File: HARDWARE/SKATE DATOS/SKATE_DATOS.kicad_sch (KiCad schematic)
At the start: 8 parts, among them J1 MPU6050, J2 BMP280, J3 ENTRADA, SW1 INTERRUPTOR, U1 ESP32-DEVKIT-V1, U2 L7805

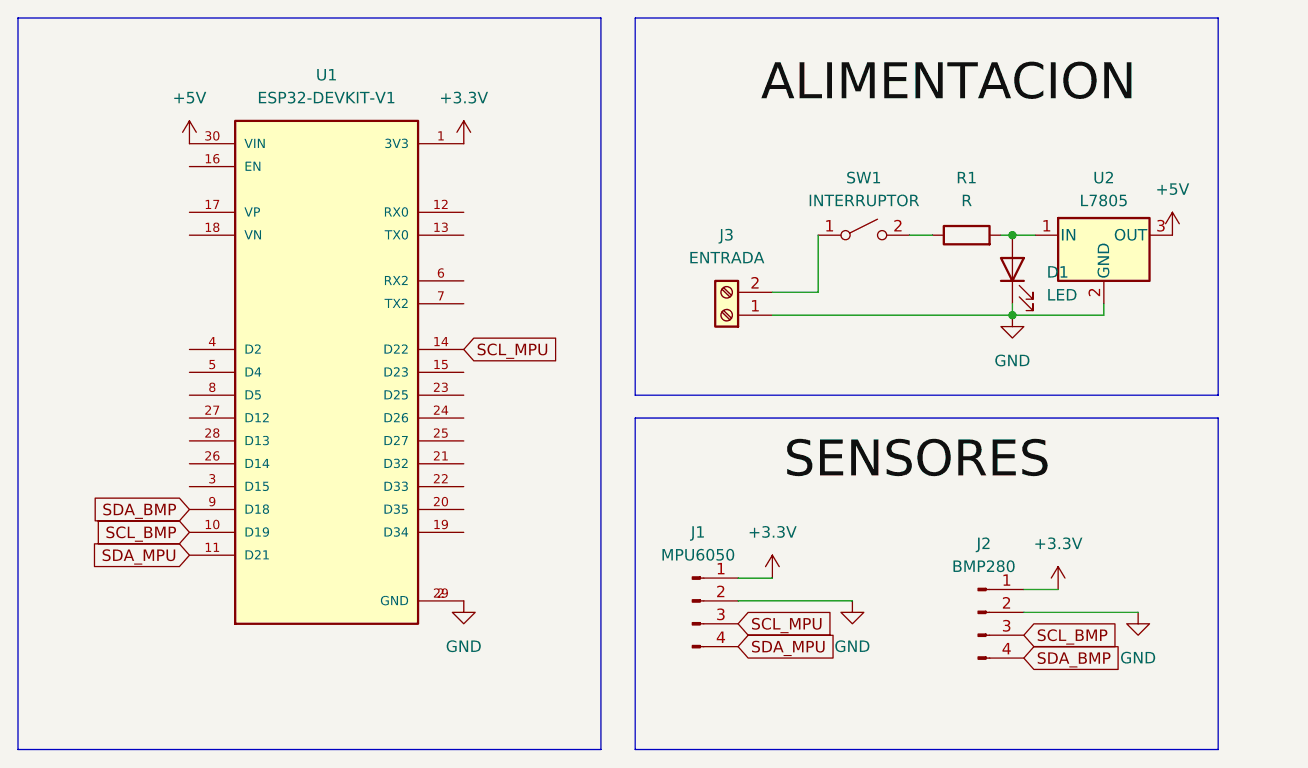
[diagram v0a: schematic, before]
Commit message: capacitores de filtro
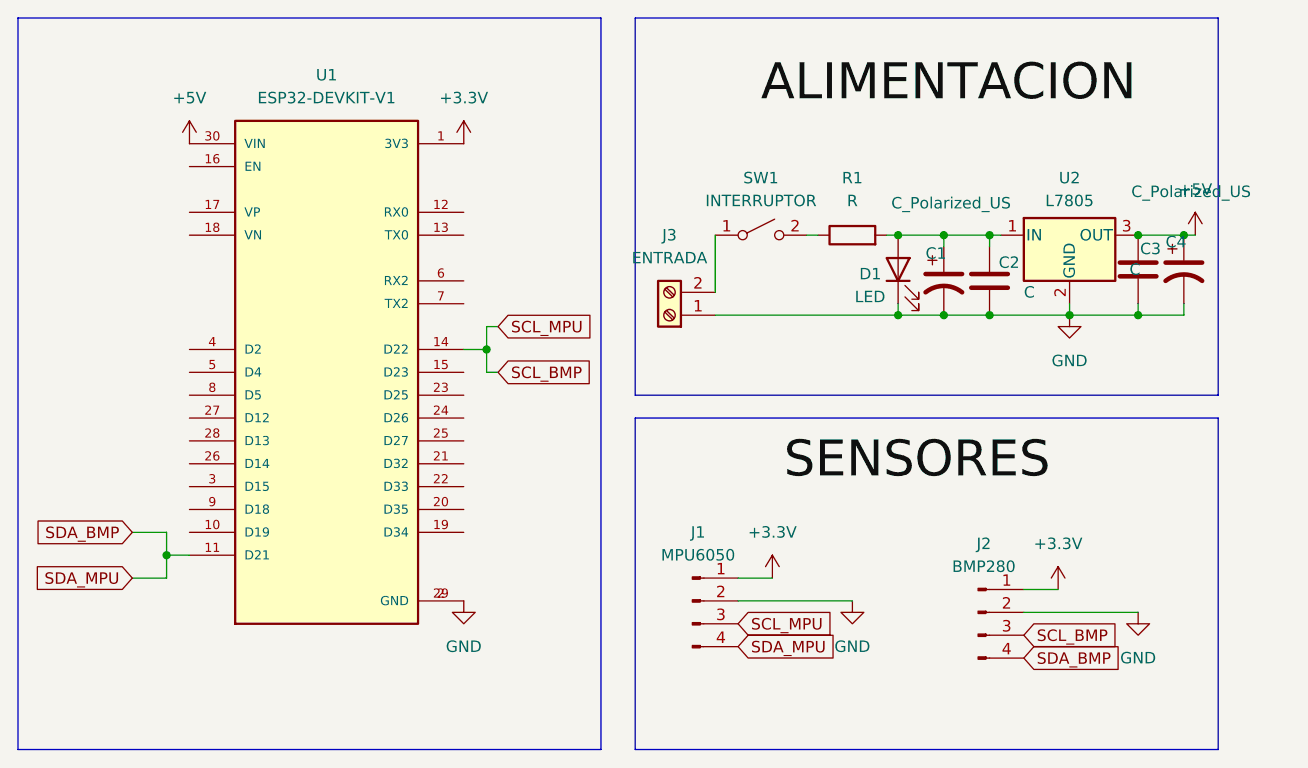
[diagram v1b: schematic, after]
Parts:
- added C1, C4: C_Polarized_US, Capacitor_THT:CP_Radial_D8.0mm_P5.00mm, symbol Device:C_Polarized_US
- added C2, C3: C, Capacitor_THT:C_Disc_D8.0mm_W2.5mm_P5.00mm, symbol Device:C
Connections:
- net SCL_MPU is gone; now on net SCL_BMP: J1.3 (Pin_3), U1.14 (D22)
- net SDA_MPU is gone; now on net SDA_BMP: J1.4 (Pin_4), U1.11 (D21)
- net +5V: now also C3.1, C4.1
- net GND: now also C1.2, C2.2, C3.2, C4.2
- net SCL_BMP: no longer U1.10 (D19)
- net SDA_BMP: no longer U1.9 (D18)
- net at D1.2 (A), R1.2, U2.1 (IN): now also C1.1, C2.1
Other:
- moved on the sheet: D1, J3, R1, SW1, U2
